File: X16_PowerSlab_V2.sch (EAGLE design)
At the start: 42 parts, among them J1 CONN_796636-3, J2 CONN_796636-3, J3 CONN_ET60T

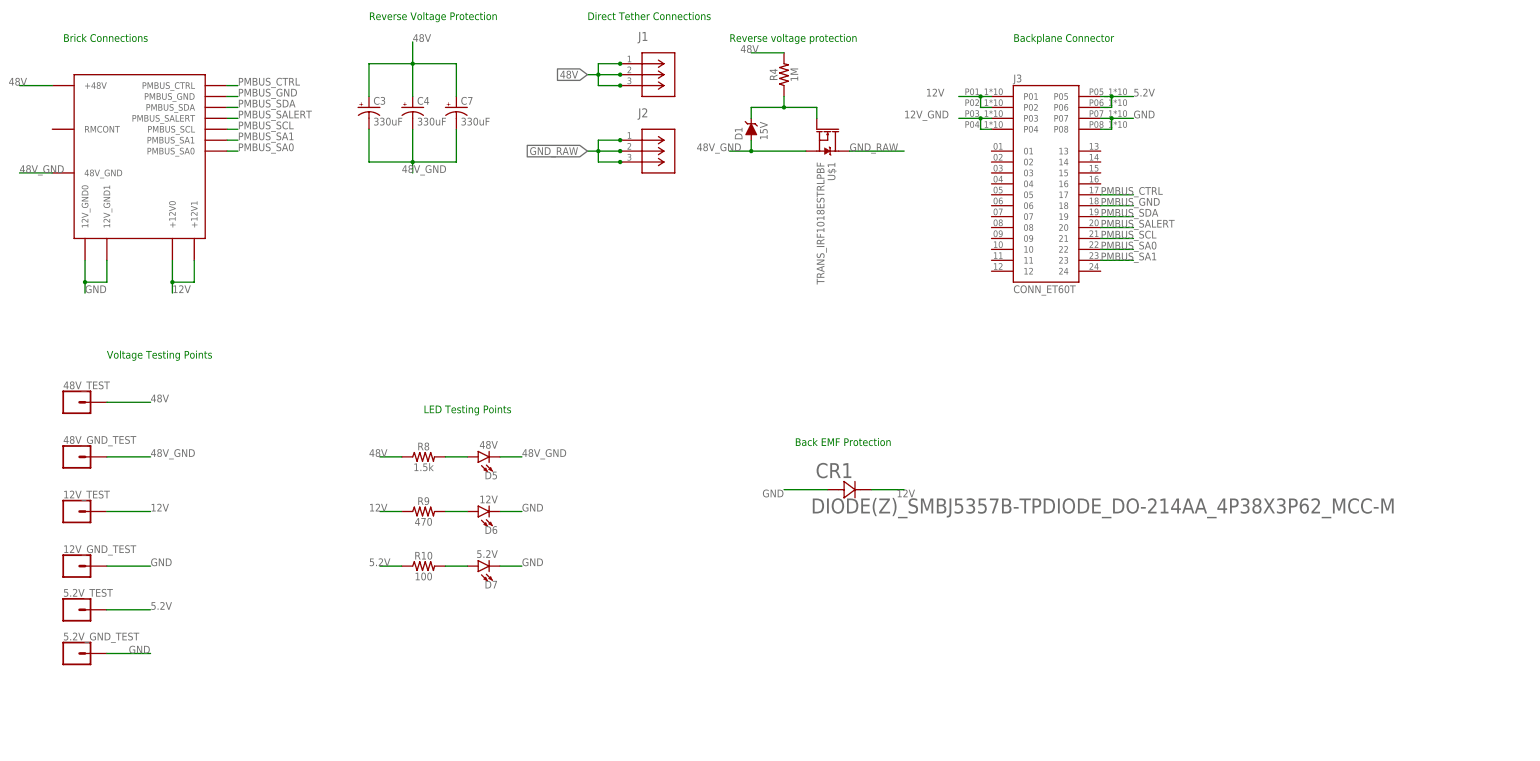
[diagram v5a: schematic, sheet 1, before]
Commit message: set up polygons
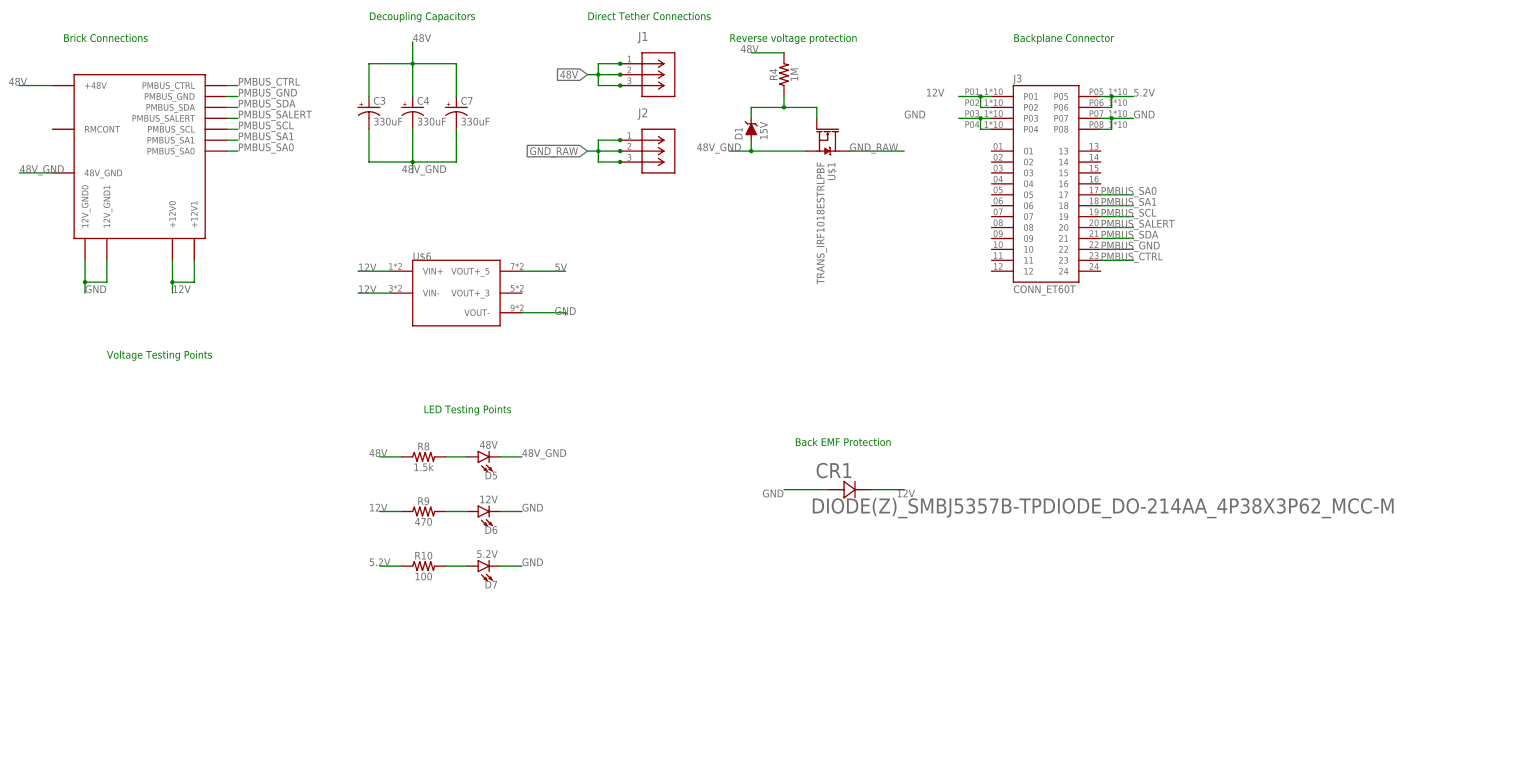
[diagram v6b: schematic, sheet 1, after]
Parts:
- removed 12V_GND_TEST, 12V_TEST, 48V_GND_TEST, 48V_TEST, 5.2V_GND_TEST, 5.2V_TEST: (no value), SparkFun-Connectors:CONN_01
- removed U$4: 5.2V_TESTPOINT, X15-Conversion-Parts-Library:5.2V_TESTPOINT
- removed U$5: 12V_TESTPOINT, X15-Conversion-Parts-Library:12V_TESTPOINT
- added 12VGND_TP, 12V_TP, 48VGND_TP, 48_TP, TP5, TP6: TEST-POINT3X5, SparkFun-Connectors:TEST-POINT3X5
- added U$6: CONN_DISTRIBUTION_TO_CONVERSION, X16_Power_Slab:CONN_DISTRIBUTION_TO_CONVERSION
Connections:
- removed net 12V_GND: J3.P03, J3.P04
- new net 5V: U$6.VOUT+_5
- net 12V: now also U$6.VIN+, U$6.VIN-; no longer 12V_TEST.1, U$5.12V
- net 48V: no longer 48V_TEST.1
- net 48V_GND: no longer 48V_GND_TEST.1
- net 5.2V: no longer 5.2V_TEST.1, U$4.5.2V
- net GND: now also J3.P03, J3.P04, U$6.VOUT-; no longer 12V_GND_TEST.1, 5.2V_GND_TEST.1
- net PMBUS_CTRL: now also J3.23; no longer J3.17
- net PMBUS_GND: now also J3.22; no longer J3.18
- net PMBUS_SA0: now also J3.17; no longer J3.22
- net PMBUS_SA1: now also J3.18; no longer J3.23
- net PMBUS_SCL: now also J3.19; no longer J3.21
- net PMBUS_SDA: now also J3.21; no longer J3.19
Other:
- note added: "Decoupling Capacitors"
- note removed: "Reverse Voltage Protection"

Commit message: updated routing
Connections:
- removed net 5V: U$6.VOUT+_5
- new net VIN: CIN1.+, CIN2.1, D4.C, U$2.VIN
- net 12V: no longer CIN1.+, CIN2.1, D4.C, U$2.VIN
- net 5.2V: now also U$6.VOUT+_5
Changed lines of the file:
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@@
 <label x="264.16" y="154.94" size="1.778" layer="95"/>
+</segment>
+<segment>
+<pinref part="U$6" gate="G$1" pin="VOUT+_5"/>
+<wire x1="121.92" y1="114.3" x2="132.08" y2="114.3" width="0.1524" layer="91"/>
+<label x="129.54" y="114.3" size="1.778" layer="95"/>
 </segment>
 </net>
@@
 <wire x1="256.54" y1="132.08" x2="264.16" y2="132.08" width="0.1524" layer="91"/>
 <label x="256.54" y="132.08" size="1.778" layer="95"/>
-</segment>
-</net>
-<net name="5V" class="0">
-<segment>
-<pinref part="U$6" gate="G$1" pin="VOUT+_5"/>
-<wire x1="121.92" y1="114.3" x2="132.08" y2="114.3" width="0.1524" layer="91"/>
-<label x="129.54" y="114.3" size="1.778" layer="95"/>
 </segment>
 </net>
@@
 </net>
 <net name="12V" class="0">
-<segment>
-<pinref part="CIN2" gate="G$1" pin="1"/>
-<wire x1="-48.26" y1="68.58" x2="-48.26" y2="71.12" width="0.1524" layer="91"/>
-<pinref part="CIN1" gate="G$1" pin="+"/>
-<wire x1="-60.96" y1="68.58" x2="-60.96" y2="71.12" width="0.1524" layer="91"/>
-<pinref part="U$2" gate="G$1" pin="VIN"/>
-<wire x1="-60.96" y1="71.12" x2="-48.26" y2="71.12" width="0.1524" layer="91"/>
-<junction x="-60.96" y="71.12"/>
-<junction x="-48.26" y="71.12"/>
-<wire x1="-48.26" y1="71.12" x2="-15.24" y2="71.12" width="0.1524" layer="91"/>
-<wire x1="-60.96" y1="71.12" x2="-68.58" y2="71.12" width="0.1524" layer="91"/>
-<pinref part="D4" gate="G$1" pin="C"/>
-</segment>
 <segment>
 <pinref part="R5" gate="G$1" pin="1"/>
@@
 </segment>
 </net>
+<net name="VIN" class="0">
+<segment>
+<pinref part="CIN2" gate="G$1" pin="1"/>
+<wire x1="-48.26" y1="68.58" x2="-48.26" y2="71.12" width="0.1524" layer="91"/>
+<pinref part="CIN1" gate="G$1" pin="+"/>
+<wire x1="-60.96" y1="68.58" x2="-60.96" y2="71.12" width="0.1524" layer="91"/>
+<pinref part="U$2" gate="G$1" pin="VIN"/>
+<wire x1="-60.96" y1="71.12" x2="-48.26" y2="71.12" width="0.1524" layer="91"/>
+<junction x="-60.96" y="71.12"/>
+<junction x="-48.26" y="71.12"/>
+<wire x1="-48.26" y1="71.12" x2="-15.24" y2="71.12" width="0.1524" layer="91"/>
+<wire x1="-60.96" y1="71.12" x2="-68.58" y2="71.12" width="0.1524" layer="91"/>
+<pinref part="D4" gate="G$1" pin="C"/>
+</segment>
+</net>

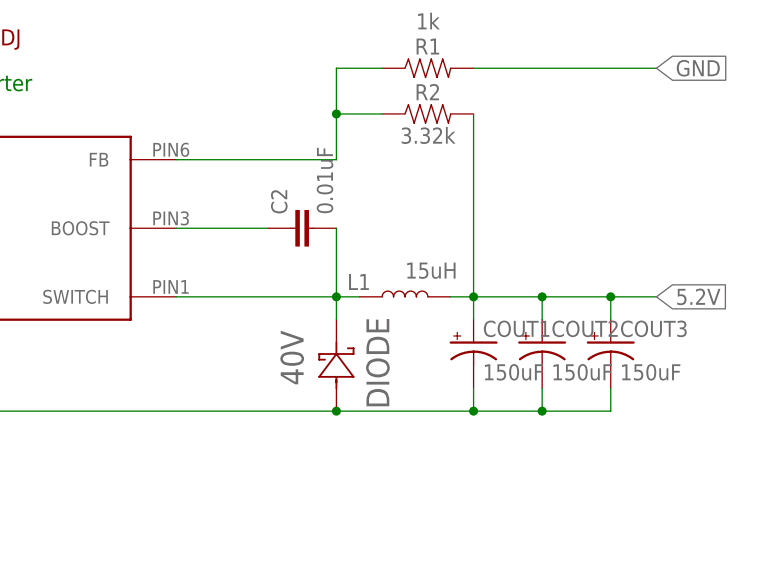
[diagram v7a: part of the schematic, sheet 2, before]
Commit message: routing, fixed outdated components
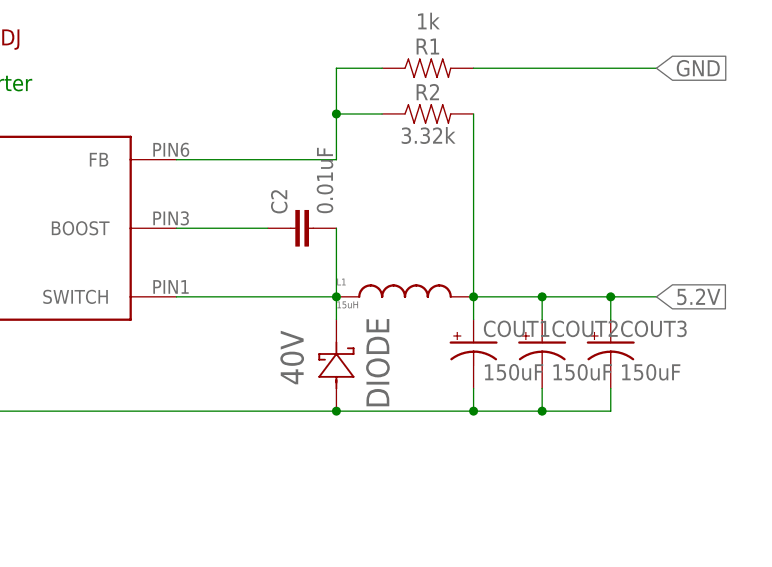
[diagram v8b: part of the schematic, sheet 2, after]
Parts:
- CR1: value DIODE(Z)_SMBJ5357B-TPDIODE_DO-214AA_4P38X3P62_MCC-M -> SMBJ12CA; device X15_Brickstribution:DIODE(Z)_SMBJ5357B-TPDIODE_DO-214AA_4P38X3P62_MCC-M -> X16_Power_Slab:SMBJ12CA
- L1: device SparkFun-Coils:2.2μH_SHIELDED_INDUCTOR -> X15-Conversion-Parts-Library:HCMA1305
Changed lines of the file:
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@@
 <part name="CIN2" library="SparkFun-Capacitors" library_urn="urn:adsk.eagle:library:510" deviceset="0.1UF" device="-0603-25V-(+80/-20%)" package3d_urn="urn:adsk.eagle:package:41385090/1" value="0.47uF"/>
 <part name="C2" library="SparkFun-Capacitors" library_urn="urn:adsk.eagle:library:510" deviceset="0.1UF" device="-0603-25V-(+80/-20%)" package3d_urn="urn:adsk.eagle:package:41385090/1" value="0.01uF"/>
-<part name="L1" library="SparkFun-Coils" library_urn="urn:adsk.eagle:library:512" deviceset="2.2μH_SHIELDED_INDUCTOR" device="" package3d_urn="urn:adsk.eagle:package:41390597/1" value="15uH"/>
 <part name="COUT1" library="SparkFun-Capacitors" library_urn="urn:adsk.eagle:library:510" deviceset="10UF-POLAR" device="-0603-6.3V-20%(TANT)" package3d_urn="urn:adsk.eagle:package:41385074/1" value="150uF"/>
 <part name="COUT2" library="SparkFun-Capacitors" library_urn="urn:adsk.eagle:library:510" deviceset="10UF-POLAR" device="-0603-6.3V-20%(TANT)" package3d_urn="urn:adsk.eagle:package:41385074/1" value="150uF"/>
@@
 <part name="D7" library="SparkFun-LED" library_urn="urn:adsk.eagle:library:529" deviceset="LED" device="0603" package3d_urn="urn:adsk.eagle:package:39354/2" value="5.2V"/>
 <part name="U$3" library="X16_Power_Slab" deviceset="CONN_BMR480_BRICK" device=""/>
-<part name="CR1" library="X15_Brickstribution" deviceset="DIODE(Z)_SMBJ5357B-TP" device="DIODE_DO-214AA_4P38X3P62_MCC-M"/>
+<part name="CR1" library="X16_Power_Slab" deviceset="SMBJ12CA" device=""/>
 <part name="C3" library="SparkFun-Capacitors" library_urn="urn:adsk.eagle:library:510" deviceset="10UF-POLAR" device="-0603-6.3V-20%(TANT)" package3d_urn="urn:adsk.eagle:package:41385074/1" value="330uF"/>
 <part name="C4" library="SparkFun-Capacitors" library_urn="urn:adsk.eagle:library:510" deviceset="10UF-POLAR" device="-0603-6.3V-20%(TANT)" package3d_urn="urn:adsk.eagle:package:41385074/1" value="330uF"/>
@@
 <part name="TP5" library="SparkFun-Connectors" library_urn="urn:adsk.eagle:library:513" deviceset="TEST-POINT" device="3X5" package3d_urn="urn:adsk.eagle:package:38285/2"/>
 <part name="TP6" library="SparkFun-Connectors" library_urn="urn:adsk.eagle:library:513" deviceset="TEST-POINT" device="3X5" package3d_urn="urn:adsk.eagle:package:38285/2"/>
+<part name="L1" library="X15-Conversion-Parts-Library" deviceset="HCMA1305" device="" package3d_urn="urn:adsk.eagle:package:24201702/2" value="15uH"/>
 </parts>
 <sheets>
@@
 <segment>
 <pinref part="CR1" gate="A" pin="1"/>
-<wire x1="203.2" y1="63.5" x2="210.82" y2="63.5" width="0.1524" layer="91"/>
+<wire x1="205.74" y1="63.5" x2="210.82" y2="63.5" width="0.1524" layer="91"/>
 <label x="213.36" y="63.5" size="1.778" layer="95" rot="R180"/>
 </segment>
@@
 <attribute name="VALUE" x="50.419" y="65.024" size="1.778" layer="96" font="vector" rot="R90"/>
 </instance>
-<instance part="L1" gate="G$1" x="58.42" y="55.88" smashed="yes" rot="R90">
-<attribute name="NAME" x="54.61" y="58.42" size="1.778" layer="95" font="vector" rot="R180"/>
-<attribute name="VALUE" x="58.42" y="59.69" size="1.778" layer="96" font="vector" align="top-left"/>
-</instance>
 <instance part="COUT1" gate="G$1" x="66.04" y="50.8" smashed="yes">
 <attribute name="NAME" x="67.056" y="51.435" size="1.778" layer="95" font="vector"/>
@@
 <attribute name="NAME" x="71.12" y="-27.94" size="1.778" layer="95" font="vector"/>
 <attribute name="VALUE" x="71.12" y="-33.02" size="1.778" layer="96" font="vector"/>
+</instance>
+<instance part="L1" gate="G$1" x="50.8" y="55.88" smashed="yes">
+<attribute name="NAME" x="50.8" y="57.15" size="0.762" layer="95"/>
+<attribute name="VALUE" x="50.8" y="54.61" size="0.762" layer="96"/>
 </instance>
 </instances>
@@
 <segment>
 <pinref part="U$2" gate="G$1" pin="SWITCH"/>
-<pinref part="L1" gate="G$1" pin="1"/>
 <wire x1="33.02" y1="55.88" x2="50.8" y2="55.88" width="0.1524" layer="91"/>
 <pinref part="C2" gate="G$1" pin="2"/>
-<wire x1="50.8" y1="55.88" x2="53.34" y2="55.88" width="0.1524" layer="91"/>
 <wire x1="50.8" y1="63.5" x2="50.8" y2="55.88" width="0.1524" layer="91"/>
 <junction x="50.8" y="55.88"/>
 <pinref part="DIODE" gate="A" pin="1"/>
 <wire x1="50.8" y1="55.88" x2="50.8" y2="53.34" width="0.1524" layer="91"/>
+<pinref part="L1" gate="G$1" pin="1"/>
 </segment>
 </net>
@@
 <net name="5.2V" class="0">
 <segment>
-<pinref part="L1" gate="G$1" pin="2"/>
-<wire x1="63.5" y1="55.88" x2="66.04" y2="55.88" width="0.1524" layer="91"/>
 <pinref part="COUT1" gate="G$1" pin="+"/>
 <wire x1="66.04" y1="55.88" x2="73.66" y2="55.88" width="0.1524" layer="91"/>
@@
 <wire x1="66.04" y1="76.2" x2="66.04" y2="55.88" width="0.1524" layer="91"/>
 <label x="86.36" y="55.88" size="1.778" layer="95" xref="yes"/>
-</segment>
-<segment>
+<pinref part="L1" gate="G$1" pin="2"/>
+</segment>
+<segment>
